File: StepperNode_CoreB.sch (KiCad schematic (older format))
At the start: 1 part

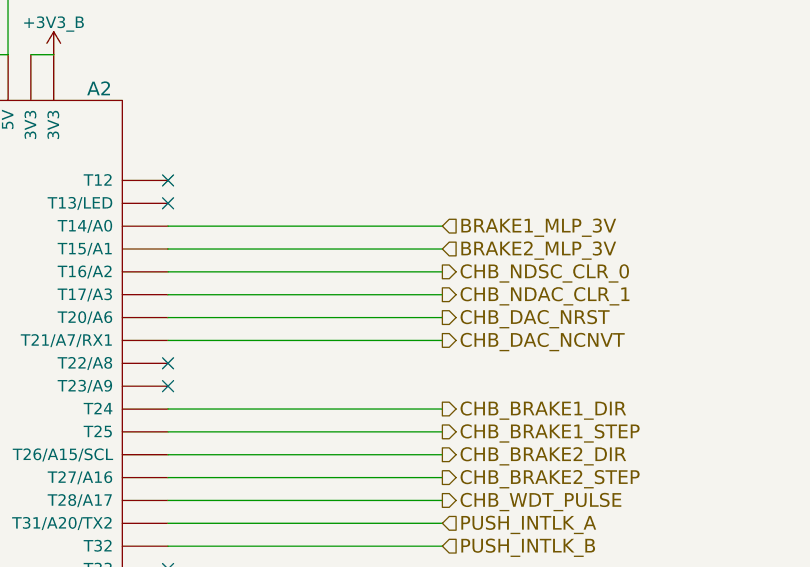
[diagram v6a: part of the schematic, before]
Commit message: Finish isolation and add brake limit switches.
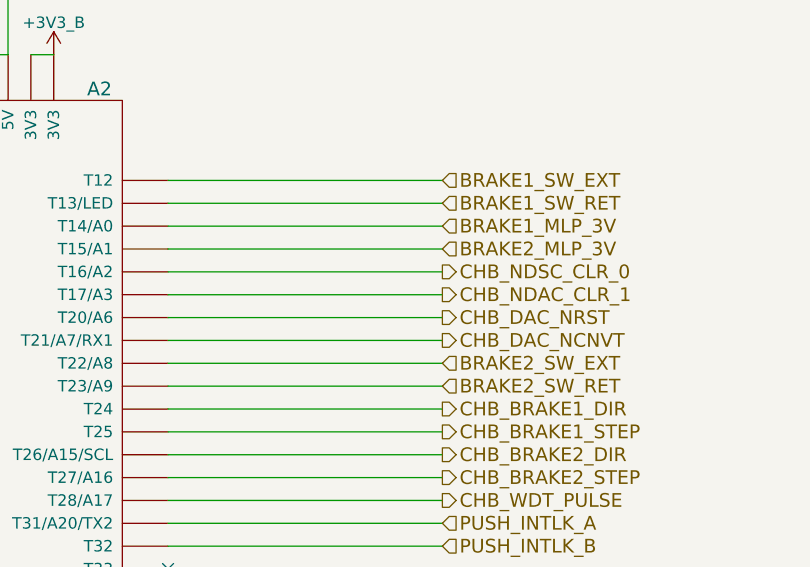
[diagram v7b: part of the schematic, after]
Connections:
- net BRAKE1_SW_EXT: now reaches A2.T12
- net BRAKE1_SW_RET: now reaches A2.T13 (T13/LED)
- net BRAKE2_SW_EXT: now reaches A2.T22 (T22/A8)
- net BRAKE2_SW_RET: now reaches A2.T23 (T23/A9)
- no-connect marks 19 -> 15
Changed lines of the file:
@@
 BRAKE2_MLP_3V
 $Comp
-L GNDD #PWR0214
+L GNDD #PWR254
 U 1 1 576221C2
 P 8050 6700
-F 0 "#PWR0214" H 8050 6450 50  0001 C CNN
+F 0 "#PWR254" H 8050 6450 50  0001 C CNN
 F 1 "GNDD" H 8050 6550 50  0000 C CNN
 F 2 "" H 8050 6700 50  0000 C CNN
@@
 $EndComp
 $Comp
-L GNDA #PWR0215
+L GNDA #PWR256
 U 1 1 576221C8
 P 8250 6750
-F 0 "#PWR0215" H 8250 6500 50  0001 C CNN
+F 0 "#PWR256" H 8250 6500 50  0001 C CNN
 F 1 "GNDA" H 8250 6600 50  0000 C CNN
 F 2 "" H 8250 6750 50  0000 C CNN
@@
 IB_FR_RX_3V
 $Comp
-L +3V3_B #PWR0216
+L +3V3_B #PWR257
 U 1 1 57671EAB
 P 8400 3450
-F 0 "#PWR0216" H 8400 3300 50  0001 C CNN
+F 0 "#PWR257" H 8400 3300 50  0001 C CNN
 F 1 "+3V3_B" H 8400 3590 50  0000 C CNN
 F 2 "" H 8400 3450 60  0000 C CNN
@@
 $EndComp
 $Comp
-L +5V_B #PWR0217
+L +5V_B #PWR255
 U 1 1 57671EC2
 P 8200 3200
-F 0 "#PWR0217" H 8200 3050 50  0001 C CNN
+F 0 "#PWR255" H 8200 3050 50  0001 C CNN
 F 1 "+5V_B" H 8200 3340 50  0000 C CNN
 F 2 "" H 8200 3200 60  0000 C CNN
@@
 $EndComp
 $Comp
-L +24V_B #PWR0218
+L +24V_B #PWR253
 U 1 1 57671ED8
 P 8000 3000
-F 0 "#PWR0218" H 8000 2850 50  0001 C CNN
+F 0 "#PWR253" H 8000 2850 50  0001 C CNN
 F 1 "+24V_B" H 8000 3140 50  0000 C CNN
 F 2 "" H 8000 3000 60  0000 C CNN
@@
 	1    0    0    -1
 $EndComp
-NoConn ~ 8900 4000
-NoConn ~ 8900 4100
-NoConn ~ 8900 4800
-NoConn ~ 8900 4900
 NoConn ~ 8900 5700
 NoConn ~ 8900 6200
@@
 NoConn ~ 8900 6000
 NoConn ~ 8900 6100
+Wire Wire Line
+	10100 4000 8900 4000
+Wire Wire Line
+	10100 4100 8900 4100
+Text HLabel 10100 4000 2    60   Input ~ 0
+BRAKE1_SW_EXT
+Text HLabel 10100 4100 2    60   Input ~ 0
+BRAKE1_SW_RET
+Wire Wire Line
+	10100 4800 8900 4800
+Wire Wire Line
+	10100 4900 8900 4900
+Text HLabel 10100 4800 2    60   Input ~ 0
+BRAKE2_SW_EXT
+Text HLabel 10100 4900 2    60   Input ~ 0
+BRAKE2_SW_RET
 $EndSCHEMATC
